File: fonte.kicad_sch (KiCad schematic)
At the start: 27 parts, among them T1 Transformer_1P_SS, U1 L7805, U2 L7905, U3 LM317_TO-220, U4 ICM7555xP, U5 ADG417BN

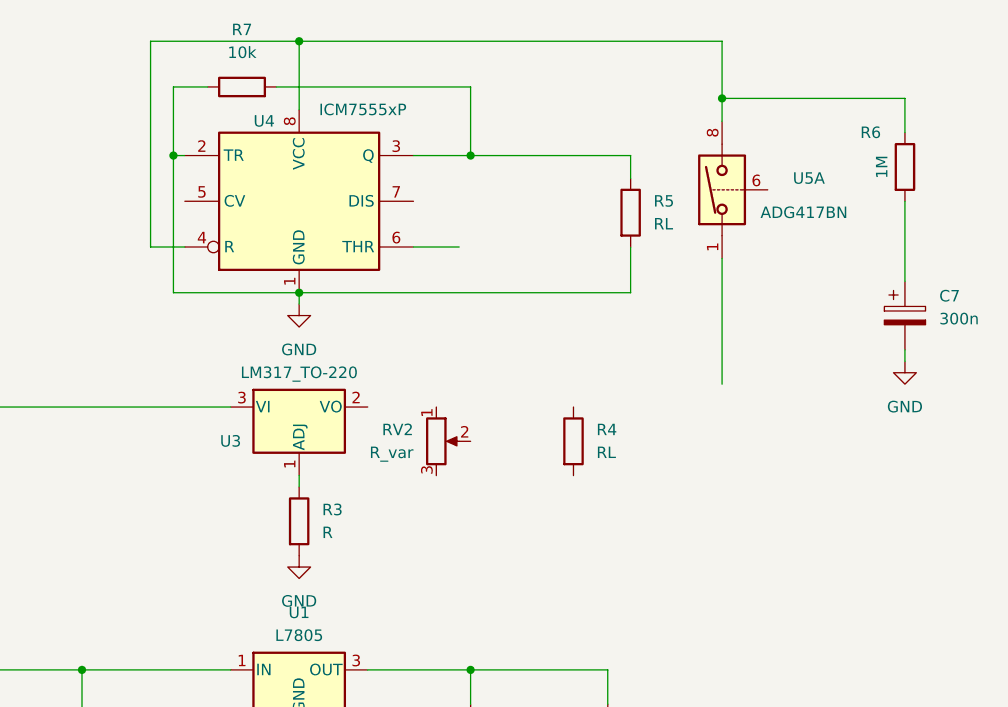
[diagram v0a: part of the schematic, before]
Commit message: Added the remaining connections to the 555
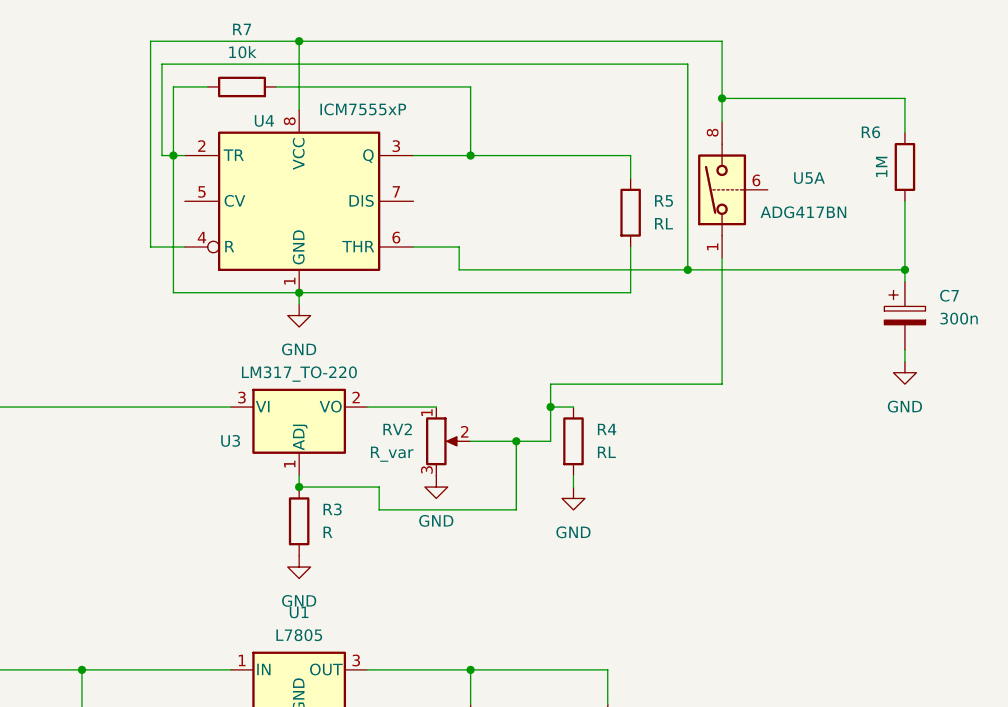
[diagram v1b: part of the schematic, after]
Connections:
- net GND: now also C7.1, R4.2, R6.2, RV2.3, U4.6 (THR)
- net at U5.1: now also R3.1, R4.1, RV2.2, U3.1 (ADJ)
- net at RV2.1: now also U3.2 (VO)
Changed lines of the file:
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@@
   (junction (at 62.23 85.09) (diameter 0) (color 0 0 0 0)
   )
+  (junction (at 210.82 40.64) (diameter 0) (color 0 0 0 0)
+  )
+  (junction (at 234.95 40.64) (diameter 0) (color 0 0 0 0)
+  )
+  (junction (at 191.77 59.69) (diameter 0) (color 0 0 0 0)
+  )
   (junction (at 121.92 114.3) (diameter 0) (color 0 0 0 0)
   )
+  (junction (at 195.58 55.88) (diameter 0) (color 0 0 0 0)
+  )
+  (junction (at 167.64 64.77) (diameter 0) (color 0 0 0 0)
+  )
   (junction (at 186.69 85.09) (diameter 0) (color 0 0 0 0)
   )
@@
     (stroke (width 0) (type default))
   )
+  (wire (pts (xy 234.95 40.64) (xy 234.95 41.91))
+    (stroke (width 0) (type default))
+  )
   (wire (pts (xy 201.93 85.09) (xy 186.69 85.09))
     (stroke (width 0) (type default))
@@
     (stroke (width 0) (type default))
   )
+  (wire (pts (xy 210.82 17.78) (xy 210.82 40.64))
+    (stroke (width 0) (type default))
+  )
+  (wire (pts (xy 186.69 59.69) (xy 191.77 59.69))
+    (stroke (width 0) (type default))
+  )
   (wire (pts (xy 96.52 95.25) (xy 99.06 95.25))
     (stroke (width 0) (type default))
@@
     (stroke (width 0) (type default))
   )
+  (wire (pts (xy 175.26 55.88) (xy 182.88 55.88))
+    (stroke (width 0) (type default))
+  )
   (wire (pts (xy 121.92 114.3) (xy 132.08 114.3))
     (stroke (width 0) (type default))
@@
     (stroke (width 0) (type default))
   )
+  (wire (pts (xy 195.58 59.69) (xy 195.58 55.88))
+    (stroke (width 0) (type default))
+  )
+  (wire (pts (xy 176.53 64.77) (xy 167.64 64.77))
+    (stroke (width 0) (type default))
+  )
   (wire (pts (xy 99.06 114.3) (xy 96.52 114.3))
     (stroke (width 0) (type default))
@@
     (stroke (width 0) (type default))
   )
+  (wire (pts (xy 234.95 25.4) (xy 234.95 21.59))
+    (stroke (width 0) (type default))
+  )
+  (wire (pts (xy 185.42 38.1) (xy 185.42 40.64))
+    (stroke (width 0) (type default))
+  )
+  (wire (pts (xy 170.18 99.06) (xy 163.83 99.06))
+    (stroke (width 0) (type default))
+  )
+  (wire (pts (xy 143.51 85.09) (xy 160.02 85.09))
+    (stroke (width 0) (type default))
+  )
+  (wire (pts (xy 57.15 85.09) (xy 62.23 85.09))
+    (stroke (width 0) (type default))
+  )
+  (wire (pts (xy 132.08 114.3) (xy 143.51 114.3))
+    (stroke (width 0) (type default))
+  )
+  (wire (pts (xy 62.23 85.09) (xy 68.58 85.09))
+    (stroke (width 0) (type default))
+  )
+  (wire (pts (xy 143.51 111.76) (xy 143.51 114.3))
+    (stroke (width 0) (type default))
+  )
+  (wire (pts (xy 152.4 17.78) (xy 210.82 17.78))
+    (stroke (width 0) (type default))
+  )
+  (wire (pts (xy 191.77 59.69) (xy 195.58 59.69))
+    (stroke (width 0) (type default))
+  )
+  (wire (pts (xy 88.9 90.17) (xy 91.44 90.17))
+    (stroke (width 0) (type default))
+  )
+  (wire (pts (xy 201.93 99.06) (xy 186.69 99.06))
+    (stroke (width 0) (type default))
+  )
+  (wire (pts (xy 121.92 85.09) (xy 132.08 85.09))
+    (stroke (width 0) (type default))
+  )
+  (wire (pts (xy 201.93 110.49) (xy 201.93 114.3))
+    (stroke (width 0) (type default))
+  )
+  (wire (pts (xy 195.58 53.34) (xy 195.58 55.88))
+    (stroke (width 0) (type default))
+  )
+  (wire (pts (xy 132.08 111.76) (xy 132.08 114.3))
+    (stroke (width 0) (type default))
+  )
+  (wire (pts (xy 186.69 85.09) (xy 186.69 88.9))
+    (stroke (width 0) (type default))
+  )
+  (wire (pts (xy 175.26 85.09) (xy 186.69 85.09))
+    (stroke (width 0) (type default))
+  )
+  (wire (pts (xy 160.02 55.88) (xy 121.92 55.88))
+    (stroke (width 0) (type default))
+  )
+  (wire (pts (xy 88.9 95.25) (xy 96.52 95.25))
+    (stroke (width 0) (type default))
+  )
+  (wire (pts (xy 153.67 27.94) (xy 152.4 27.94))
+    (stroke (width 0) (type default))
+  )
+  (wire (pts (xy 151.13 15.24) (xy 167.64 15.24))
+    (stroke (width 0) (type default))
+  )
+  (wire (pts (xy 191.77 67.31) (xy 176.53 67.31))
+    (stroke (width 0) (type default))
+  )
+  (wire (pts (xy 62.23 85.09) (xy 62.23 87.63))
+    (stroke (width 0) (type default))
+  )
+  (wire (pts (xy 185.42 40.64) (xy 210.82 40.64))
+    (stroke (width 0) (type default))
+  )
+  (wire (pts (xy 167.64 92.71) (xy 167.64 96.52))
+    (stroke (width 0) (type default))
+  )
+  (wire (pts (xy 132.08 99.06) (xy 132.08 104.14))
+    (stroke (width 0) (type default))
+  )
+  (wire (pts (xy 154.94 27.94) (xy 153.67 27.94))
+    (stroke (width 0) (type default))
+  )
   (wire (pts (xy 180.34 38.1) (xy 185.42 38.1))
     (stroke (width 0) (type default))
   )
-  (wire (pts (xy 234.95 25.4) (xy 234.95 21.59))
-    (stroke (width 0) (type default))
-  )
-  (wire (pts (xy 170.18 99.06) (xy 163.83 99.06))
-    (stroke (width 0) (type default))
-  )
-  (wire (pts (xy 143.51 85.09) (xy 160.02 85.09))
-    (stroke (width 0) (type default))
-  )
-  (wire (pts (xy 57.15 85.09) (xy 62.23 85.09))
-    (stroke (width 0) (type default))
-  )
-  (wire (pts (xy 132.08 114.3) (xy 143.51 114.3))
-    (stroke (width 0) (type default))
-  )
-  (wire (pts (xy 62.23 85.09) (xy 68.58 85.09))
-    (stroke (width 0) (type default))
-  )
-  (wire (pts (xy 143.51 111.76) (xy 143.51 114.3))
-    (stroke (width 0) (type default))
-  )
-  (wire (pts (xy 88.9 90.17) (xy 91.44 90.17))
-    (stroke (width 0) (type default))
-  )
-  (wire (pts (xy 201.93 99.06) (xy 186.69 99.06))
-    (stroke (width 0) (type default))
-  )
-  (wire (pts (xy 121.92 85.09) (xy 132.08 85.09))
-    (stroke (width 0) (type default))
-  )
-  (wire (pts (xy 201.93 110.49) (xy 201.93 114.3))
-    (stroke (width 0) (type default))
-  )
-  (wire (pts (xy 132.08 111.76) (xy 132.08 114.3))
-    (stroke (width 0) (type default))
-  )
-  (wire (pts (xy 186.69 85.09) (xy 186.69 88.9))
-    (stroke (width 0) (type default))
-  )
-  (wire (pts (xy 175.26 85.09) (xy 186.69 85.09))
-    (stroke (width 0) (type default))
-  )
-  (wire (pts (xy 160.02 55.88) (xy 121.92 55.88))
-    (stroke (width 0) (type default))
-  )
-  (wire (pts (xy 88.9 95.25) (xy 96.52 95.25))
-    (stroke (width 0) (type default))
-  )
-  (wire (pts (xy 151.13 15.24) (xy 167.64 15.24))
-    (stroke (width 0) (type default))
-  )
-  (wire (pts (xy 62.23 85.09) (xy 62.23 87.63))
-    (stroke (width 0) (type default))
-  )
-  (wire (pts (xy 167.64 92.71) (xy 167.64 96.52))
-    (stroke (width 0) (type default))
-  )
-  (wire (pts (xy 132.08 99.06) (xy 132.08 104.14))
-    (stroke (width 0) (type default))
-  )
-  (wire (pts (xy 154.94 27.94) (xy 153.67 27.94))
+  (wire (pts (xy 214.63 53.34) (xy 195.58 53.34))
     (stroke (width 0) (type default))
   )
@@
     (stroke (width 0) (type default))
   )
+  (wire (pts (xy 210.82 40.64) (xy 234.95 40.64))
+    (stroke (width 0) (type default))
+  )
+  (wire (pts (xy 191.77 59.69) (xy 191.77 67.31))
+    (stroke (width 0) (type default))
+  )
   (wire (pts (xy 109.22 114.3) (xy 121.92 114.3))
     (stroke (width 0) (type default))
@@
     (stroke (width 0) (type default))
   )
+  (wire (pts (xy 198.12 63.5) (xy 198.12 64.77))
+    (stroke (width 0) (type default))
+  )
   (wire (pts (xy 143.51 114.3) (xy 162.56 114.3))
     (stroke (width 0) (type default))
@@
     (stroke (width 0) (type default))
   )
+  (wire (pts (xy 152.4 27.94) (xy 152.4 17.78))
+    (stroke (width 0) (type default))
+  )
   (wire (pts (xy 45.72 85.09) (xy 49.53 85.09))
     (stroke (width 0) (type default))
@@
     (stroke (width 0) (type default))
   )
+  (wire (pts (xy 176.53 67.31) (xy 176.53 64.77))
+    (stroke (width 0) (type default))
+  )
   (wire (pts (xy 121.92 55.88) (xy 121.92 85.09))
     (stroke (width 0) (type default))
@@
     (stroke (width 0) (type default))
   )
+  (wire (pts (xy 195.58 55.88) (xy 198.12 55.88))
+    (stroke (width 0) (type default))
+  )
   (wire (pts (xy 204.47 38.1) (xy 204.47 43.18))
     (stroke (width 0) (type default))
@@
     (stroke (width 0) (type default))
   )
-  (wire (pts (xy 234.95 33.02) (xy 234.95 41.91))
+  (wire (pts (xy 234.95 33.02) (xy 234.95 40.64))
     (stroke (width 0) (type default))
   )
@@
         (path "/3badeb0e-f6a7-4733-beae-e79d572ba060"
           (reference "#PWR06") (unit 1)
+        )
+      )
+    )
+  )
+  (symbol (lib_id "power:GND") (at 182.88 63.5 0) (unit 1)
+    (in_bom yes) (on_board yes) (dnp no) (fields_autoplaced)
+    (property "Reference" "#PWR07" (at 182.88 69.85 0)
+      (effects (font (size 1.27 1.27)) hide)
+    )
+    (property "Value" "GND" (at 182.88 68.58 0)
+      (effects (font (size 1.27 1.27)))
+    )
+    (property "Footprint" "" (at 182.88 63.5 0)
+      (effects (font (size 1.27 1.27)) hide)
+    )
+    (property "Datasheet" "" (at 182.88 63.5 0)
+      (effects (font (size 1.27 1.27)) hide)
+    )
+    (pin "1")
+    (instances
+      (project "fonte"
+        (path "/3badeb0e-f6a7-4733-beae-e79d572ba060"
+          (reference "#PWR07") (unit 1)
         )
       )
@@
         )
       )
+    )
+  )
+  (symbol (lib_id "power:GND") (at 198.12 64.77 0) (unit 1)
+    (in_bom yes) (on_board yes) (dnp no) (fields_autoplaced)
+    (property "Reference" "#PWR08" (at 198.12 71.12 0)
+      (effects (font (size 1.27 1.27)) hide)
+    )
+    (property "Value" "GND" (at 198.12 69.85 0)
+      (effects (font (size 1.27 1.27)))
+    )
+    (property "Footprint" "" (at 198.12 64.77 0)
+      (effects (font (size 1.27 1.27)) hide)
+    )
+    (property "Datasheet" "" (at 198.12 64.77 0)
+      (effects (font (size 1.27 1.27)) hide)
+    )
+    (pin "1")
+    (instances
+      (project "fonte"
+        (path "/3badeb0e-f6a7-4733-beae-e79d572ba060"
+          (reference "#PWR08") (unit 1)
+        )
+      )
